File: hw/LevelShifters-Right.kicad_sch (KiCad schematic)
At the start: 9 parts, among them U1300 SN74LVCH16T245, U1301 SN74LVCH16T245, U1302 SN74LVCH16T245

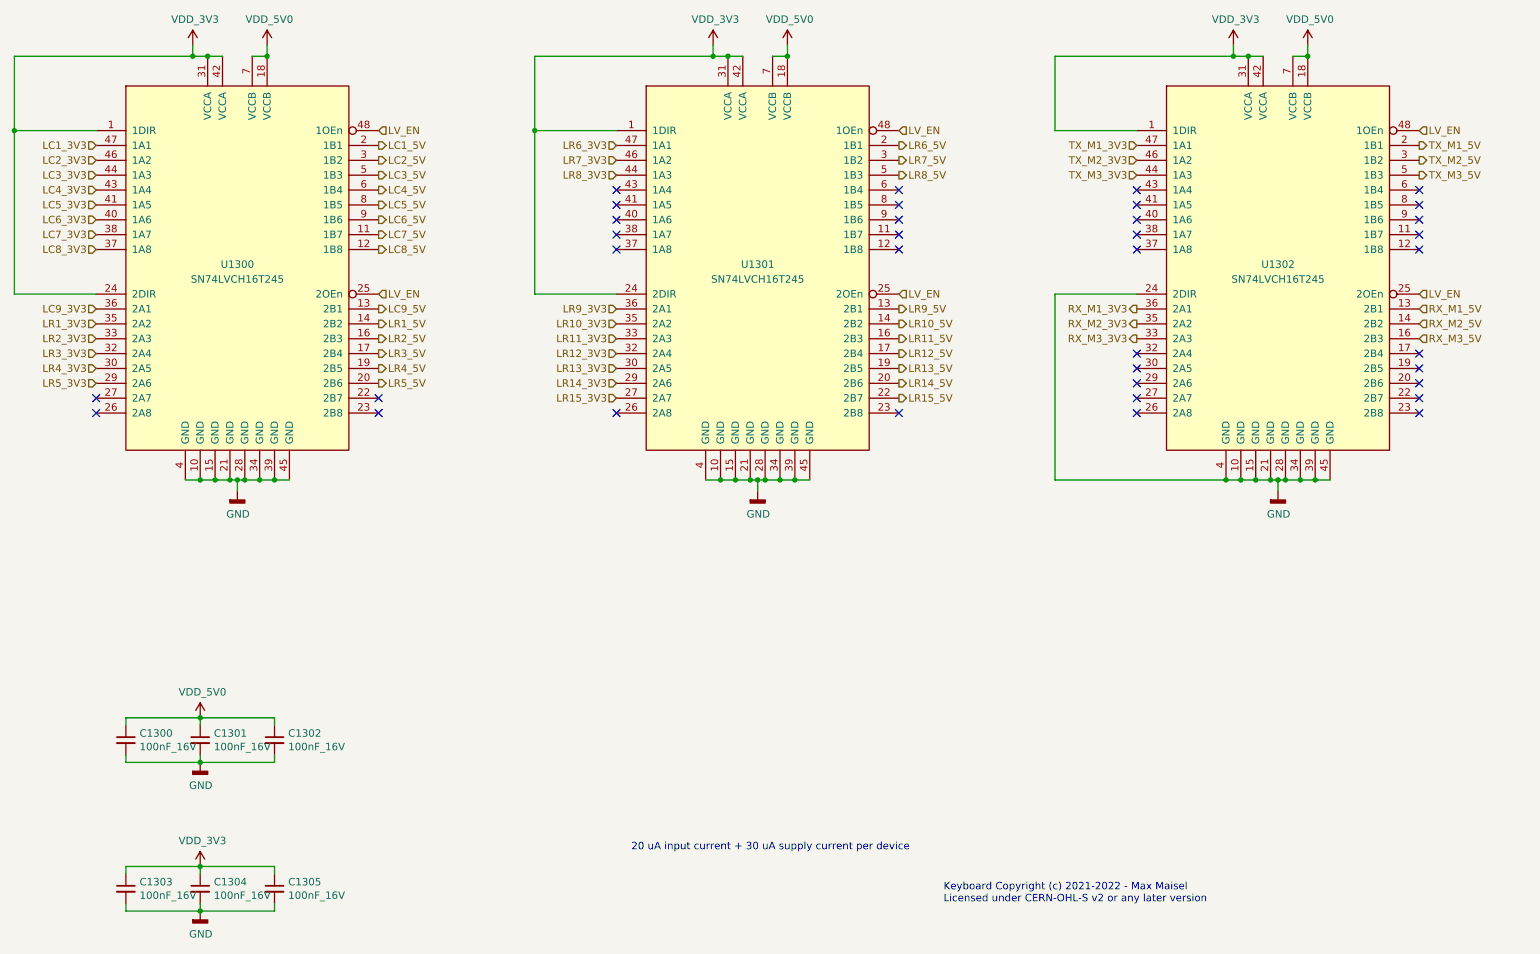
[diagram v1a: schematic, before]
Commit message: Update schematic:
- Add ESD protection.
- Adjust distance bolts so they fit to the MX mounting plate.
- Make key layout symmetric.
- Add resistor to TX driver outputs.
- Use alternate IO functions on inter-board connectors.
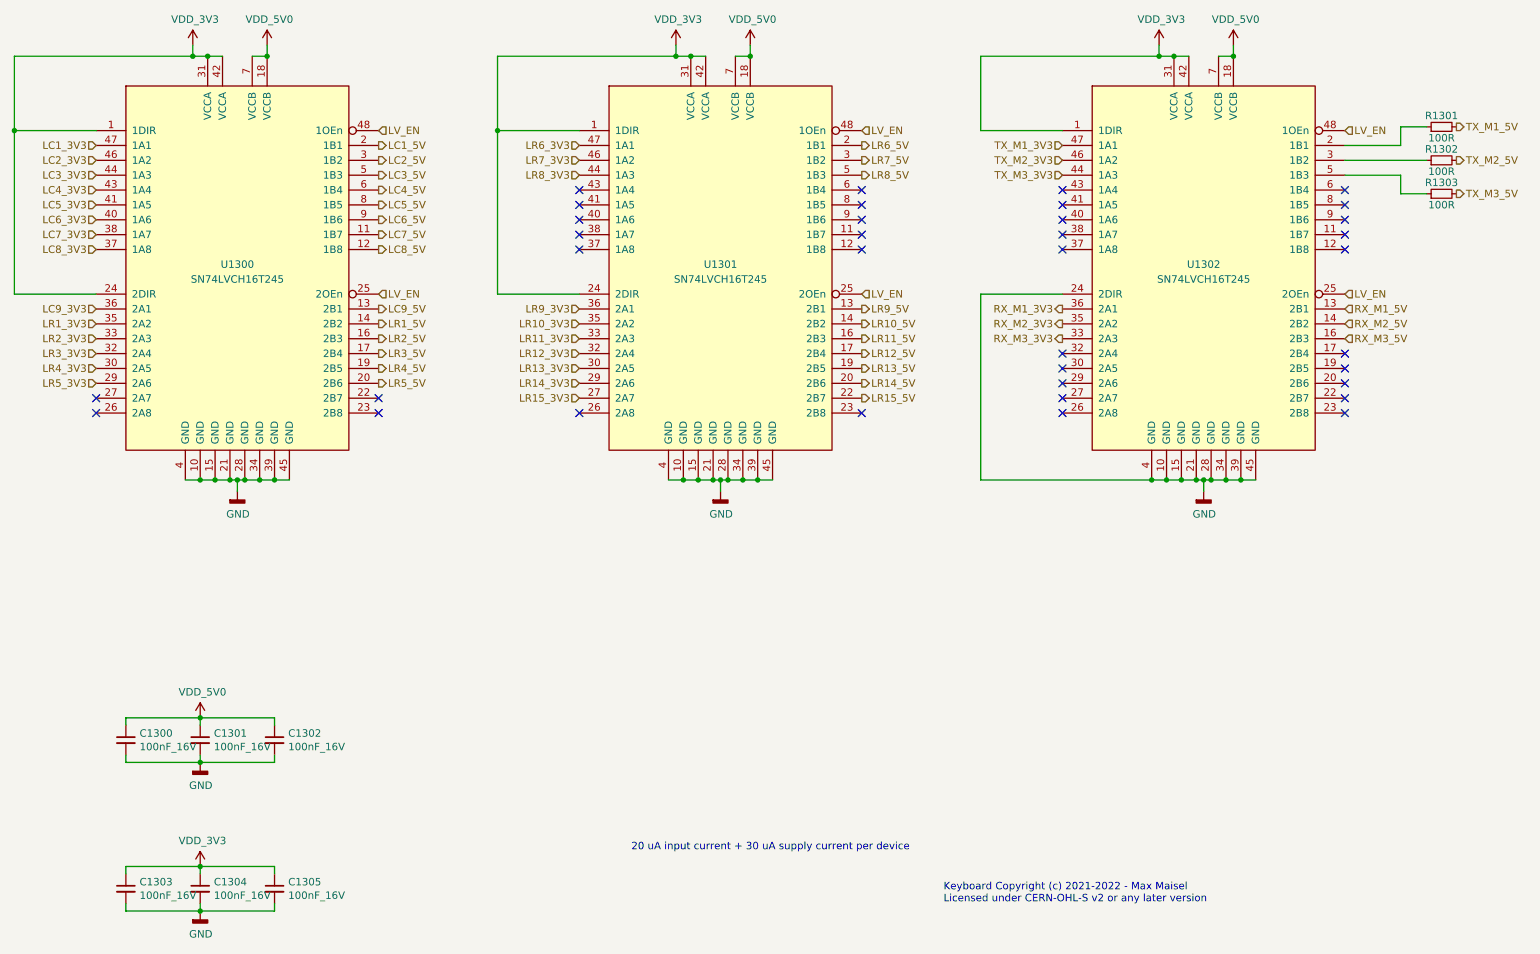
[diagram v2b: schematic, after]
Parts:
- added R1301, R1302, R1303: 100R, Keyboard:R_0402, symbol Keyboard:100R
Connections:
- net TX_M1_5V: now also R1301.2; no longer U1302.2 (1B1)
- net TX_M2_5V: now also R1302.2; no longer U1302.3 (1B2)
- net TX_M3_5V: now also R1303.2; no longer U1302.5 (1B3)
- new net: R1301.1, U1302.2 (1B1)
- new net: R1302.1, U1302.3 (1B2)
- new net: R1303.1, U1302.5 (1B3)
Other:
- moved on the sheet: U1301, U1302

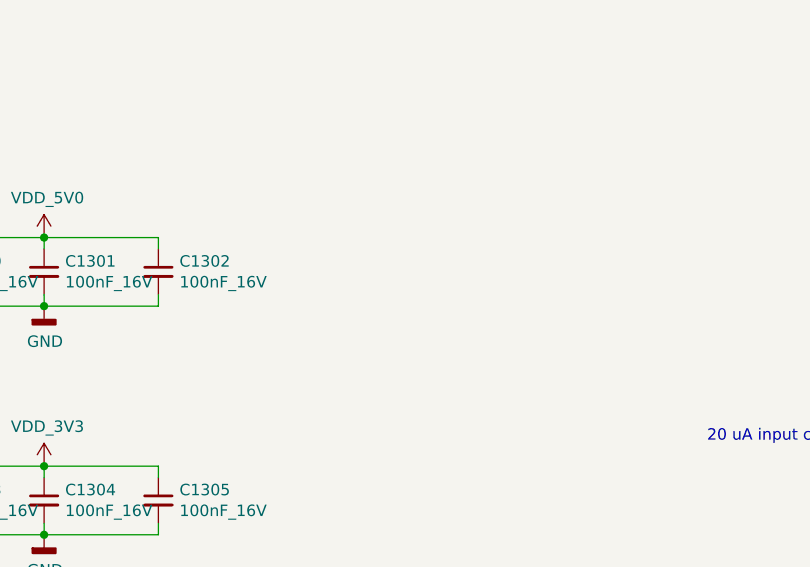
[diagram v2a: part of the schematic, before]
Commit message: Add current probes to 3.3V and pull-up to LV_EN.
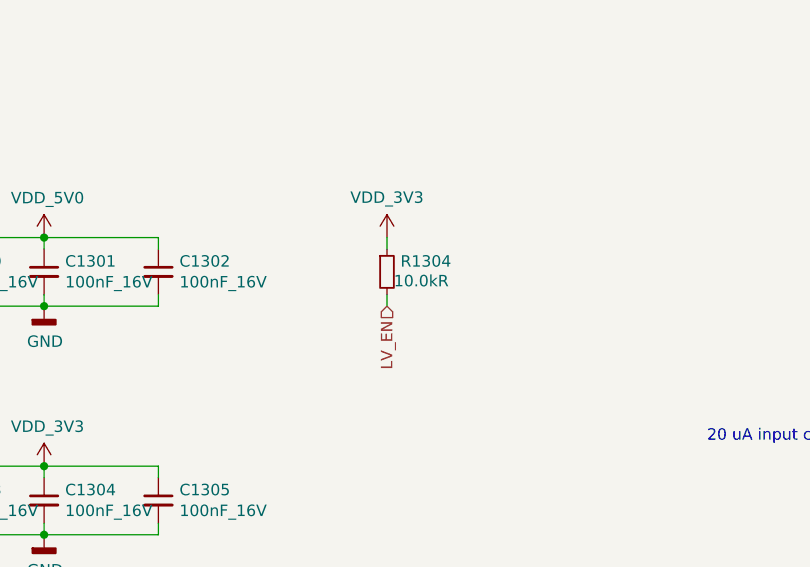
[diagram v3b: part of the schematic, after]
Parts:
- added R1304: 10.0kR, Keyboard:R_0402, symbol Keyboard:10.0kR
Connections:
- net LV_EN: now also R1304.2
- net VDD_3V3: now also R1304.1
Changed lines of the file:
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@@
+    (stroke (width 0) (type default) (color 0 0 0 0))
+  )
+  (wire (pts (xy 88.9 140.97) (xy 88.9 139.7))
     (stroke (width 0) (type default) (color 0 0 0 0))
   )
@@
   )
   (wire (pts (xy 33.02 67.31) (xy 19.05 67.31))
+    (stroke (width 0) (type default) (color 0 0 0 0))
+  )
+  (wire (pts (xy 88.9 146.05) (xy 88.9 147.32))
     (stroke (width 0) (type default) (color 0 0 0 0))
   )
@@
   (hierarchical_label "TX_M2_5V" (shape output) (at 265.43 44.45 0)
     (effects (font (size 1.27 1.27)) (justify left))
+  )
+  (hierarchical_label "LV_EN" (shape input) (at 88.9 147.32 270)
+    (effects (font (size 1.27 1.27)) (justify right))
   )
   (hierarchical_label "LC6_3V3" (shape input) (at 33.02 54.61 180)
@@
       (effects (font (size 1.27 1.27)) hide)
     )
+    (pin "1")
+  )
+  (symbol (lib_id "Keyboard:10.0kR") (at 88.9 143.51 0) (unit 1)
+    (in_bom yes) (on_board yes)
+    (property "Reference" "R1304" (id 0) (at 90.3986 142.3416 0)
+      (effects (font (size 1.27 1.27)) (justify left))
+    )
+    (property "Value" "10.0kR" (id 1) (at 89.662 144.526 0)
+      (effects (font (size 1.27 1.27)) (justify left))
+    )
+    (property "Footprint" "Keyboard:R_0402" (id 2) (at 87.122 145.542 0)
+      (effects (font (size 1.27 1.27)) hide)
+    )
+    (property "Datasheet" "667-ERJ-2RKF1002X" (id 3) (at 89.662 143.002 0)
+      (effects (font (size 1.27 1.27)) hide)
+    )
+    (property "mouser#" "667-ERJ-2RKF1002X" (id 4) (at 92.202 140.462 0)
+      (effects (font (size 1.524 1.524)) hide)
+    )
+    (pin "1")
+    (pin "2")
+  )
+  (symbol (lib_id "Keyboard:VDD_3V3") (at 88.9 139.7 0) (unit 1)
+    (in_bom yes) (on_board yes)
+    (property "Reference" "#PWR01313" (id 0) (at 88.9 143.51 0)
+      (effects (font (size 1.27 1.27)) hide)
+    )
+    (property "Value" "VDD_3V3" (id 1) (at 88.9 135.255 0))
+    (property "Footprint" "" (id 2) (at 88.9 139.7 0)
+      (effects (font (size 1.27 1.27)) hide)
+    )
+    (property "Datasheet" "" (id 3) (at 88.9 139.7 0)
+      (effects (font (size 1.27 1.27)) hide)
+    )
